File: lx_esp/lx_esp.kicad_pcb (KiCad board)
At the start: 4 copper layers, 74 x 24 mm, 26 parts, among them J1 Conn_01x02, J2 200LX_02X05, Q1 Dual_Nch_MOSFET, SW1 SW_Push, SW2 SW_SPDT, U1 LTC4365, U2 XC6210, U3 ESP-12F, U4 TRS3238E

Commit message: more pcb layout
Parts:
- C3, C5, C6, C7, C8, C9, R1, R2, R5, R6, R7, R8, U4: moved to B.Cu
- U3: footprint ESP8266:ESP-12E_SMD -> ssop_20:ESP-12E_SMD_hax
- moved C3 130.5 mm to (59.2, 27.5)
- moved C4 128.6 mm to (61.5, 30.0)
- moved C1 128.2 mm to (41.2, 34.2), turned to 90 degrees
- moved U3 127.6 mm to (81.2, 29.0)
- moved SW1 126.7 mm to (43.6, 43.0), turned to 180 degrees
- moved SW2 126.5 mm to (60.0, 41.5), turned to 90 degrees
- moved R1 126.3 mm to (50.1, 26.2)
- moved R4 126.2 mm to (41.2, 28.9), turned to 270 degrees
- moved R3 126.0 mm to (42.6, 25.2), turned to 180 degrees
- moved C2 125.2 mm to (40.2, 38.8)
- moved U2 124.1 mm to (44.8, 32.5), turned to 270 degrees
- moved R8 123.6 mm to (78.3, 32.5)
- moved Q1 123.6 mm to (51.0, 34.5)
- moved R2 123.5 mm to (41.2, 27.8), turned to 270 degrees
- moved J1 123.4 mm to (51.5, 41.0)
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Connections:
- U1 pad 6: Net-(U1-Pad6) -> (no net)
- U2 pad 3: Net-(U2-Pad3) -> (no net)
- U3 pad 11: Net-(U3-Pad11) -> (no net)
- U3 pad 17: Net-(U3-Pad17) -> (no net)
- U3 pad 18: Net-(U3-Pad18) -> (no net)
- U3 pad 19: Net-(U3-Pad19) -> (no net)
- U3 pad 20: Net-(U3-Pad20) -> (no net)
- U3 pad 21: Net-(U3-Pad21) -> (no net)
- U3 pad 22: Net-(U3-Pad22) -> (no net)
- U4 pad 10: Net-(J2-Pad8) -> Net-(J2-Pad6)
- U4 pad 12: Net-(J2-Pad9) -> Net-(J2-Pad1)
- U4 pad 14: Net-(U4-Pad14) -> (no net)
- U4 pad 15: Net-(U4-Pad15) -> (no net)
- U4 pad 16: Net-(U4-Pad16) -> (no net)
- U4 pad 17: /RI -> /CD
- U4 pad 19: /UART0_RTS -> /DSR
- U4 pad 22: /DSR -> /UART0_TXD
- U4 pad 23: /UART0_TXD -> /UART0_RTS
- U4 pad 24: /CD -> /RI
- U4 pad 5: Net-(J2-Pad1) -> Net-(J2-Pad9)
- U4 pad 6: Net-(J2-Pad2) -> Net-(J2-Pad8)
- U4 pad 7: Net-(J2-Pad6) -> Net-(J2-Pad2)
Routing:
- net Net-(R7-Pad1): track 12.1 -> 65.2 mm, vias 0 -> 1
- net /UART0_RXD: track 0.00 -> 35.0 mm, vias 0 -> 1
- net /UART0_TXD: track 0.00 -> 34.7 mm, vias 0 -> 1
- net /DTR: track 0.00 -> 32.9 mm, vias 0 -> 1
- net /CD: track 0.00 -> 30.9 mm, vias 0 -> 3
- net /RI: track 0.00 -> 28.6 mm, vias 0 -> 3
- net /UART0_RTS: track 0.00 -> 22.8 mm, vias 0 -> 1
- net /DSR: track 0.00 -> 22.7 mm, vias 0 -> 1
- net /UART0_CTS: track 0.00 -> 21.6 mm, vias 0 -> 1
- net Net-(J2-Pad3): track 0.00 -> 16.5 mm, vias 0 -> 1
- net Net-(J2-Pad4): track 0.00 -> 16.2 mm, vias 0 -> 1
- net Net-(J2-Pad8): track 0.00 -> 14.8 mm, vias 0 -> 2
- net Net-(J1-Pad2): track 53.6 -> 39.0 mm, vias 0 -> 1
- net Net-(J2-Pad2): track 0.00 -> 13.7 mm, vias 0 -> 1
- net Net-(J2-Pad9): track 0.00 -> 13.5 mm
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- added copper zone on B.Cu, net GND
- added copper zone on F.Cu, net GND
- added copper zone on In2.Cu, net GND
- added copper zone on In1.Cu, net VCC
- removed copper zone on In1.Cu, net GND
- removed copper zone on In2.Cu, net VCC
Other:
- board size 74 x 24 mm -> 60.5 x 24 mm
- net class Default: via_dia 1.2 -> 1; via_drill 0.9 -> 0.5

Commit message: pcb tweaks
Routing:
- net Net-(R7-Pad1): track 65.2 -> 56.9 mm, vias 1 -> 2
- net /CD: track 30.9 -> 30.1 mm

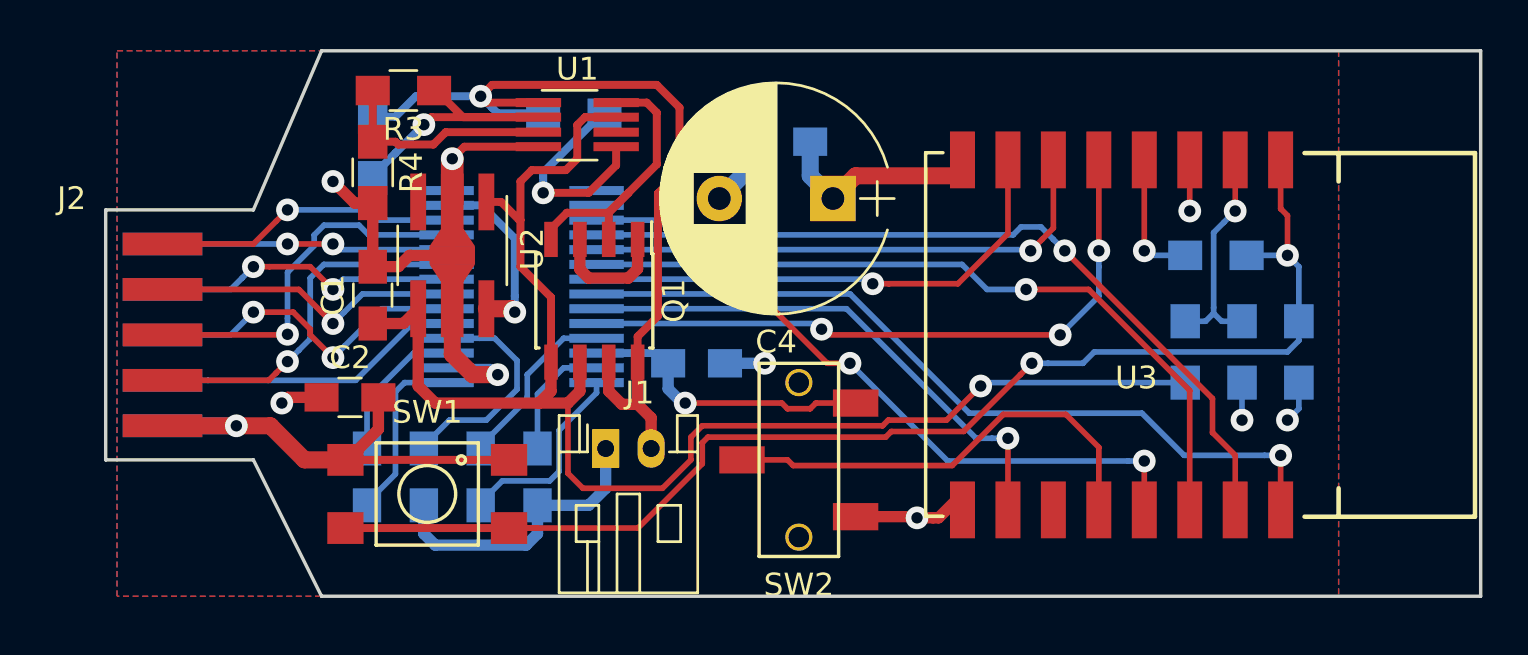
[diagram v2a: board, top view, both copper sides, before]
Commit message: narrower pcb for esp
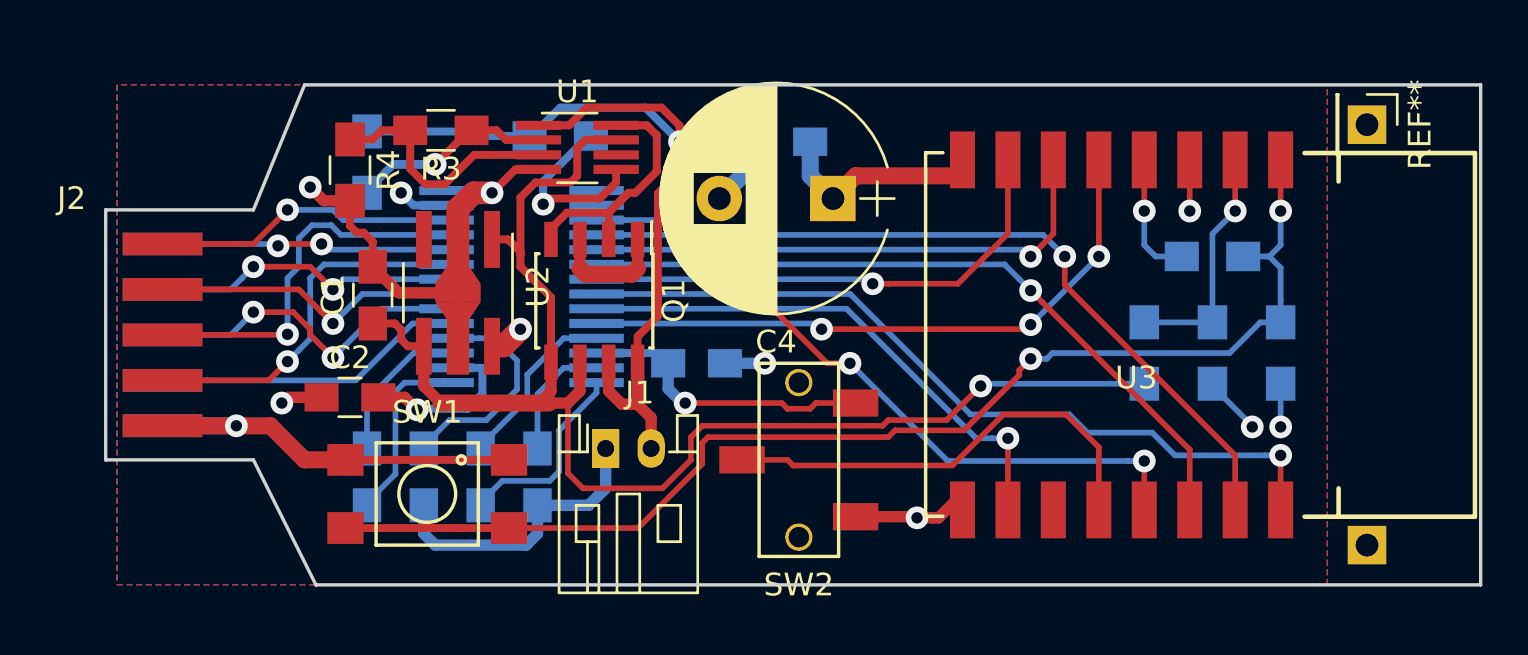
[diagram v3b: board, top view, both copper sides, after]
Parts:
- added REF**: Pin_Header_Straight_1x01_Pitch2.54mm, Pin_Headers:Pin_Header_Straight_1x01_Pitch2.54mm, F.Cu at (85.0, 26.8)
- added REF**: Pin_Header_Straight_1x01_Pitch2.54mm, Pin_Headers:Pin_Header_Straight_1x01_Pitch2.54mm, B.Cu at (85.0, 45.2)
- moved R3 2.41 mm to (44.2, 27.0)
- moved R5 1.80 mm to (75.2, 36.8)
- moved U2 1.67 mm to (45.0, 34.1)
- moved R6 1.30 mm to (78.2, 36.8)
- moved R1 1.17 mm to (49.5, 27.2)
- moved R4 1.00 mm to (40.2, 28.8)
- moved U1 1.00 mm to (50.2, 27.8)
- moved R7 0.80 mm to (81.2, 36.8)
- moved R2 0.70 mm to (41.0, 28.4)
- moved R8 0.16 mm to (78.2, 32.5)
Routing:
- net VCC: track 35.6 -> 31.3 mm, vias 5 -> 6
- net Net-(C1-Pad1): track 66.2 -> 62.4 mm
- net Net-(R2-Pad2): track 13.6 -> 10.8 mm
- net Net-(R7-Pad1): track 56.9 -> 54.8 mm
- net /DTR: track 32.9 -> 31.4 mm
- net Net-(R3-Pad2): track 9.82 -> 11.1 mm
- net /RI: track 28.3 -> 27.1 mm
- net Net-(R1-Pad2): track 9.21 -> 8.11 mm
- net Net-(J1-Pad2): track 39.0 -> 39.8 mm
- net Net-(Q1-Pad2): track 13.0 -> 12.1 mm
- net GND: track 73.4 -> 72.7 mm
- net /Vmon: track 9.23 -> 9.86 mm
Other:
- board size 60.5 x 24 mm -> 60.5 x 22 mm
